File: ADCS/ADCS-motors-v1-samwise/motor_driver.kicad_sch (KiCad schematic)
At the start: 1 part, among them J7 Conn01x07

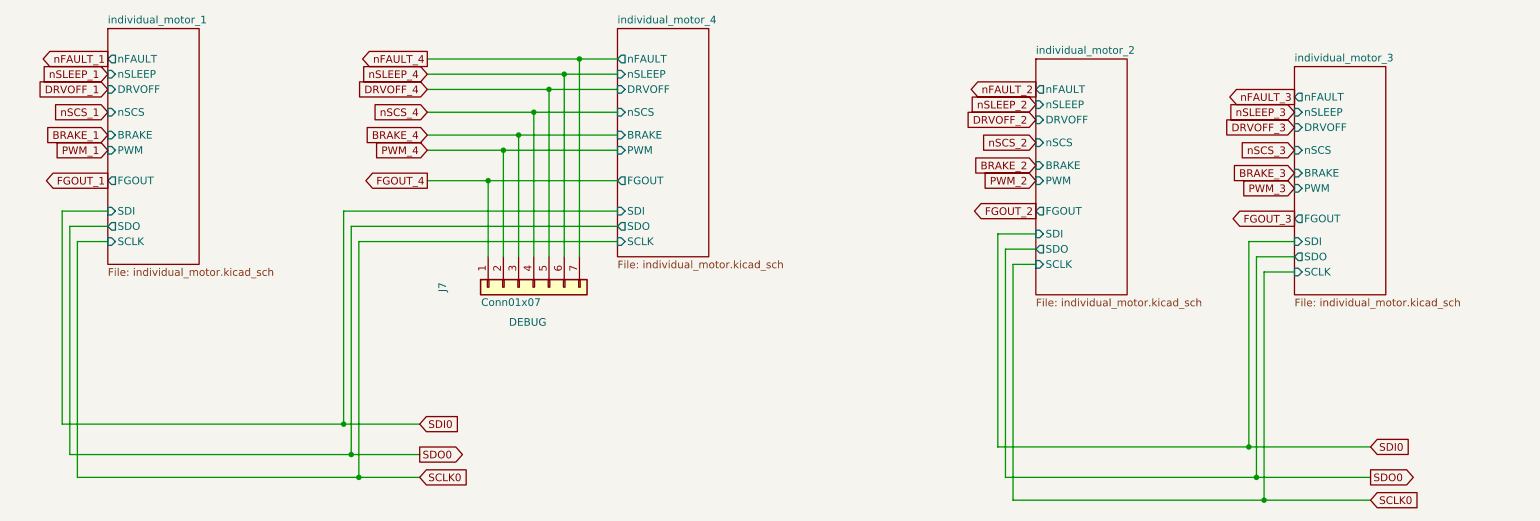
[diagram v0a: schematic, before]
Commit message: Fixed 3.3V internal regulator + added FETS
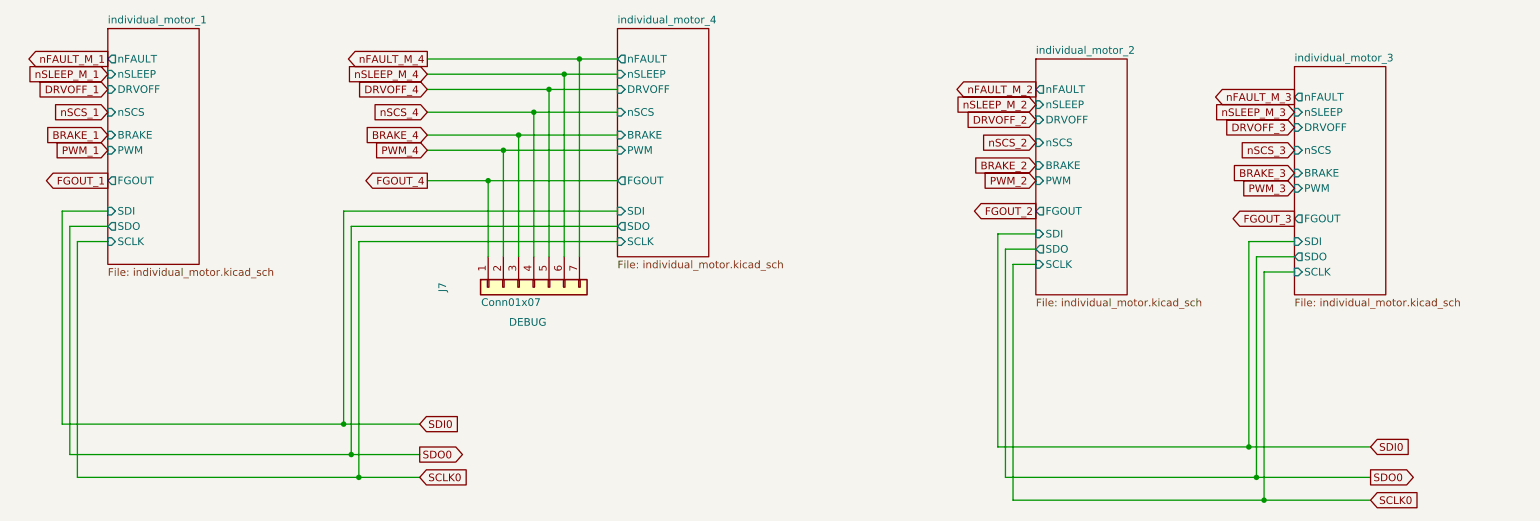
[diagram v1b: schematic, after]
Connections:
- net nFAULT_4 renamed nFAULT_M_4
- net nSLEEP_4 renamed nSLEEP_M_4
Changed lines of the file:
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@@
 	(title_block
 		(title "Reaction Wheel Motor Board")
-		(date "2025-04-07")
-		(rev "1.1")
+		(date "2025-08-27")
+		(rev "1.2")
 		(company "Stanford Student Space Initiative")
 		(comment 1 "Carson Lauer")
@@
 		)
 	)
-	(global_label "nFAULT_2"
+	(global_label "nFAULT_M_2"
 		(shape output)
 		(at 193.04 36.83 180)
@@
 		)
 		(property "Intersheetrefs" "${INTERSHEET_REFS}"
-			(at 181.8795 36.83 0)
+			(at 179.4605 36.83 0)
 			(effects
 				(font
@@
 		)
 	)
-	(global_label "nFAULT_4"
+	(global_label "nFAULT_M_4"
 		(shape output)
 		(at 91.44 31.75 180)
@@
 		)
 		(property "Intersheetrefs" "${INTERSHEET_REFS}"
-			(at 80.2795 31.75 0)
-			(effects
-				(font
-					(size 1.27 1.27)
-				)
-				(justify right)
-				(hide yes)
-			)
-		)
-	)
-	(global_label "nSLEEP_4"
+			(at 77.8605 31.75 0)
+			(effects
+				(font
+					(size 1.27 1.27)
+				)
+				(justify right)
+				(hide yes)
+			)
+		)
+	)
+	(global_label "nSLEEP_M_4"
 		(shape input)
 		(at 91.44 34.29 180)
@@
 		)
 		(property "Intersheetrefs" "${INTERSHEET_REFS}"
-			(at 79.9773 34.29 0)
+			(at 77.5583 34.29 0)
 			(effects
 				(font
@@
 		)
 	)
-	(global_label "nSLEEP_3"
+	(global_label "nSLEEP_M_3"
 		(shape input)
 		(at 236.22 40.64 180)
@@
 		)
 		(property "Intersheetrefs" "${INTERSHEET_REFS}"
-			(at 224.7573 40.64 0)
-			(effects
-				(font
-					(size 1.27 1.27)
-				)
-				(justify right)
-				(hide yes)
-			)
-		)
-	)
-	(global_label "nSLEEP_1"
+			(at 222.3383 40.64 0)
+			(effects
+				(font
+					(size 1.27 1.27)
+				)
+				(justify right)
+				(hide yes)
+			)
+		)
+	)
+	(global_label "nSLEEP_M_1"
 		(shape input)
 		(at 38.1 34.29 180)
@@
 		)
 		(property "Intersheetrefs" "${INTERSHEET_REFS}"
-			(at 26.6373 34.29 0)
+			(at 24.2183 34.29 0)
 			(effects
 				(font
@@
 		)
 	)
-	(global_label "nFAULT_3"
+	(global_label "nFAULT_M_3"
 		(shape output)
 		(at 236.22 38.1 180)
@@
 		)
 		(property "Intersheetrefs" "${INTERSHEET_REFS}"
-			(at 225.0595 38.1 0)
+			(at 222.6405 38.1 0)
 			(effects
 				(font
@@
 		)
 	)
-	(global_label "nSLEEP_2"
+	(global_label "nSLEEP_M_2"
 		(shape input)
 		(at 193.04 39.37 180)
@@
 		)
 		(property "Intersheetrefs" "${INTERSHEET_REFS}"
-			(at 181.5773 39.37 0)
+			(at 179.1583 39.37 0)
 			(effects
 				(font
@@
 		)
 	)
-	(global_label "nFAULT_1"
+	(global_label "nFAULT_M_1"
 		(shape output)
 		(at 38.1 31.75 180)
@@
 		)
 		(property "Intersheetrefs" "${INTERSHEET_REFS}"
-			(at 26.9395 31.75 0)
-			(effects
-				(font
+			(at 24.5205 31.75 0)
+			(effects
+				(font
